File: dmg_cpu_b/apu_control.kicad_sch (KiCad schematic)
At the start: 73 parts

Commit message: CH1 Regs page completed.
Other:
- company: (none) -> CC-BY-SA-4.0 Régis Galland & Michael Singer -- Derived work from Furrtek
- title: (none) -> DMG CPU B
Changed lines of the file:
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@@
 (kicad_sch (version 20211123) (generator eeschema)
   (paper "A3")
+  (title_block
+    (title "DMG CPU B")
+    (date "2022-03-12")
+    (rev "0")
+    (company "CC-BY-SA-4.0 Régis Galland & Michael Singer -- Derived work from Furrtek")
+    (comment 1 "https://github.com/msinger/dmg-schematics")
+  )
   (junction (at 300.355 128.905) (diameter 0) (color 0 0 0 0)
   )

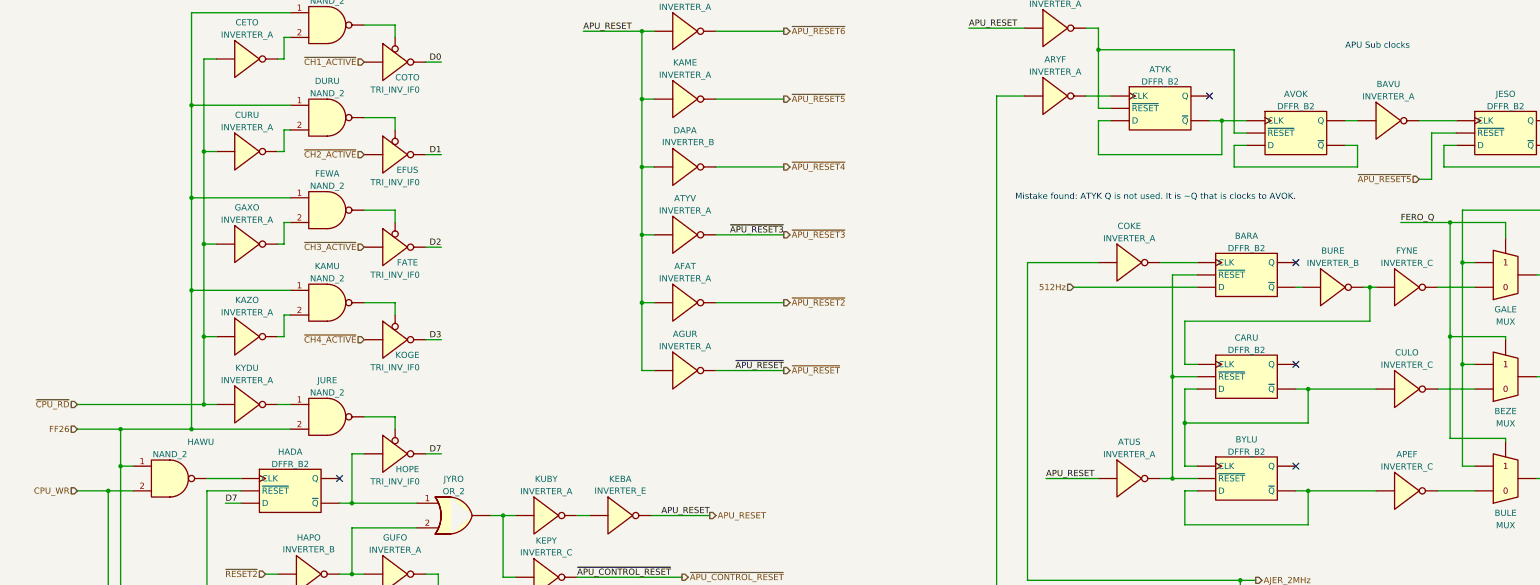
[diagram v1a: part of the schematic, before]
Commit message: CH2 Reg page added.
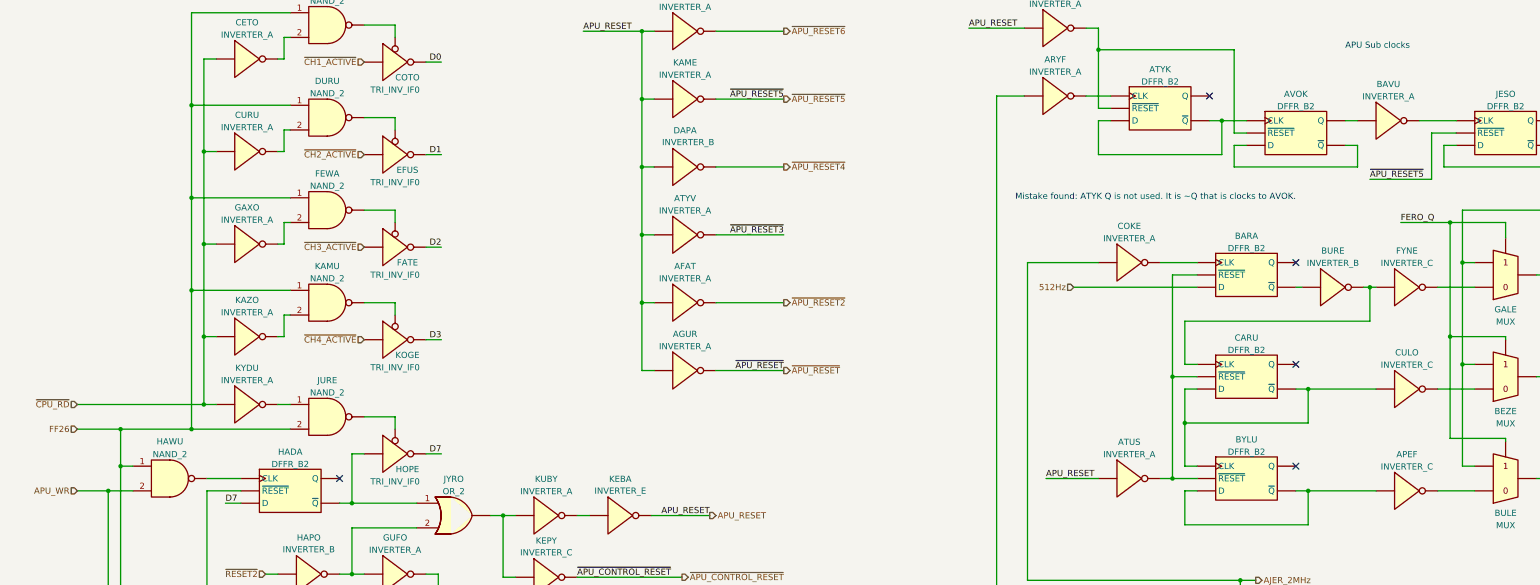
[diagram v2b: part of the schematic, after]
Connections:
- net CPU_WR renamed APU_WR
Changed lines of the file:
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@@
     (stroke (width 0) (type default) (color 0 0 0 0))
   )
-  (wire (pts (xy 323.215 85.725) (xy 325.755 85.725))
+  (wire (pts (xy 313.055 85.725) (xy 325.755 85.725))
     (stroke (width 0) (type default) (color 0 0 0 0))
   )
@@
     (effects (font (size 1.27 1.27)) (justify left bottom))
   )
+  (label "~{APU_RESET5}" (at 313.055 85.725 0)
+    (effects (font (size 1.27 1.27)) (justify left bottom))
+  )
   (label "APU_RESET" (at 177.165 154.94 180)
     (effects (font (size 1.27 1.27)) (justify right bottom))
@@
   )
   (label "D6" (at 88.9 268.605 180)
+    (effects (font (size 1.27 1.27)) (justify right bottom))
+  )
+  (label "~{APU_RESET5}" (at 192.405 69.215 180)
     (effects (font (size 1.27 1.27)) (justify right bottom))
   )
@@
     (effects (font (size 1.27 1.27)) (justify left))
   )
-  (hierarchical_label "CPU_WR" (shape input) (at 46.99 149.86 180)
+  (hierarchical_label "APU_WR" (shape input) (at 46.99 149.86 180)
     (effects (font (size 1.27 1.27)) (justify right))
   )
@@
   )
   (hierarchical_label "JESO_512K" (shape output) (at 369.57 73.66 0)
-    (effects (font (size 1.27 1.27)) (justify left))
-  )
-  (hierarchical_label "~{APU_RESET5}" (shape input) (at 323.215 85.725 180)
-    (effects (font (size 1.27 1.27)) (justify right))
-  )
-  (hierarchical_label "~{APU_RESET3}" (shape output) (at 192.405 97.155 0)
     (effects (font (size 1.27 1.27)) (justify left))
   )
@@
   (symbol (lib_id "DMG_CPU_Cells:NAND_2") (at 66.04 147.32 0) (unit 1)
     (in_bom yes) (on_board yes)
-    (property "Reference" "HAWU" (id 0) (at 72.39 139.8102 0))
+    (property "Reference" "HAWU" (id 0) (at 66.04 139.7 0))
     (property "Value" "NAND_2" (id 1) (at 66.04 142.3471 0))
     (property "Footprint" "" (id 2) (at 66.04 147.32 0)

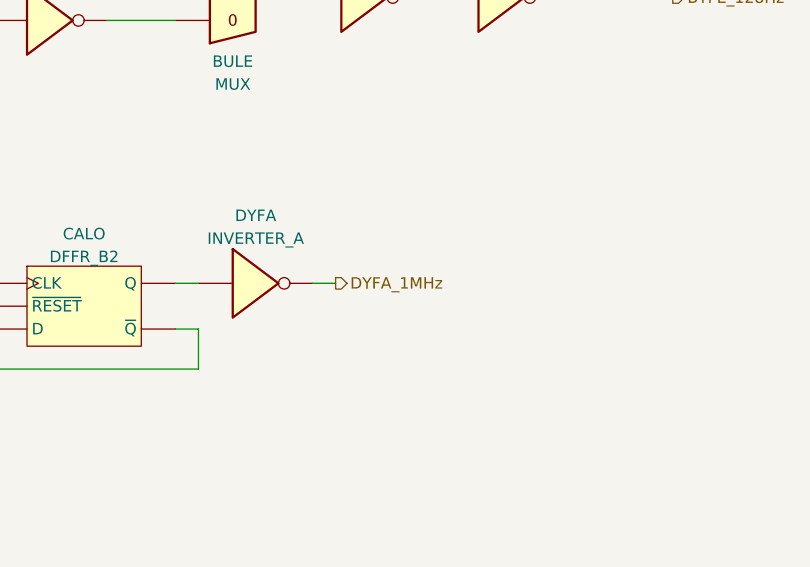
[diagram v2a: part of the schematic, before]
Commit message: channel 1 page added
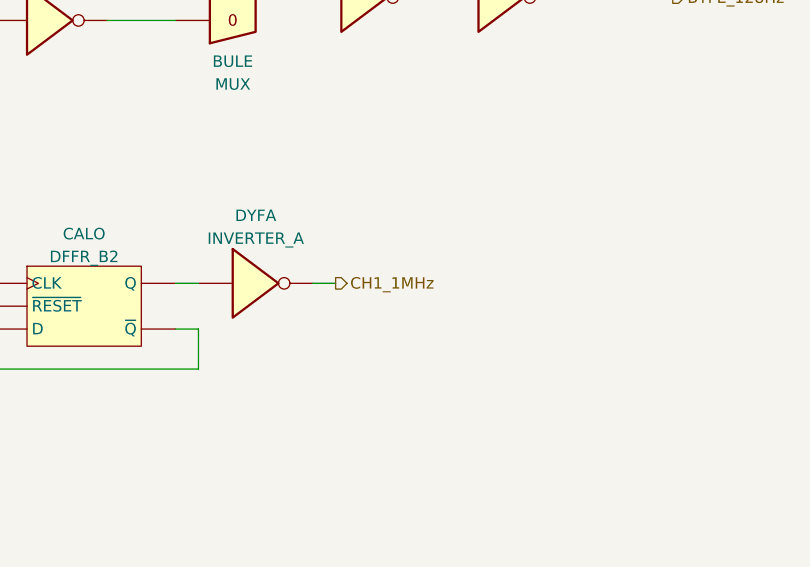
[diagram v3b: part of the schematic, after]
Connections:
- net DYFA_1MHz renamed CH1_1MHz
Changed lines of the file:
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@@
     (effects (font (size 1.27 1.27)) (justify left))
   )
-  (hierarchical_label "DYFA_1MHz" (shape output) (at 352.425 179.07 0)
+  (hierarchical_label "CH1_1MHz" (shape output) (at 352.425 179.07 0)
     (effects (font (size 1.27 1.27)) (justify left))
   )

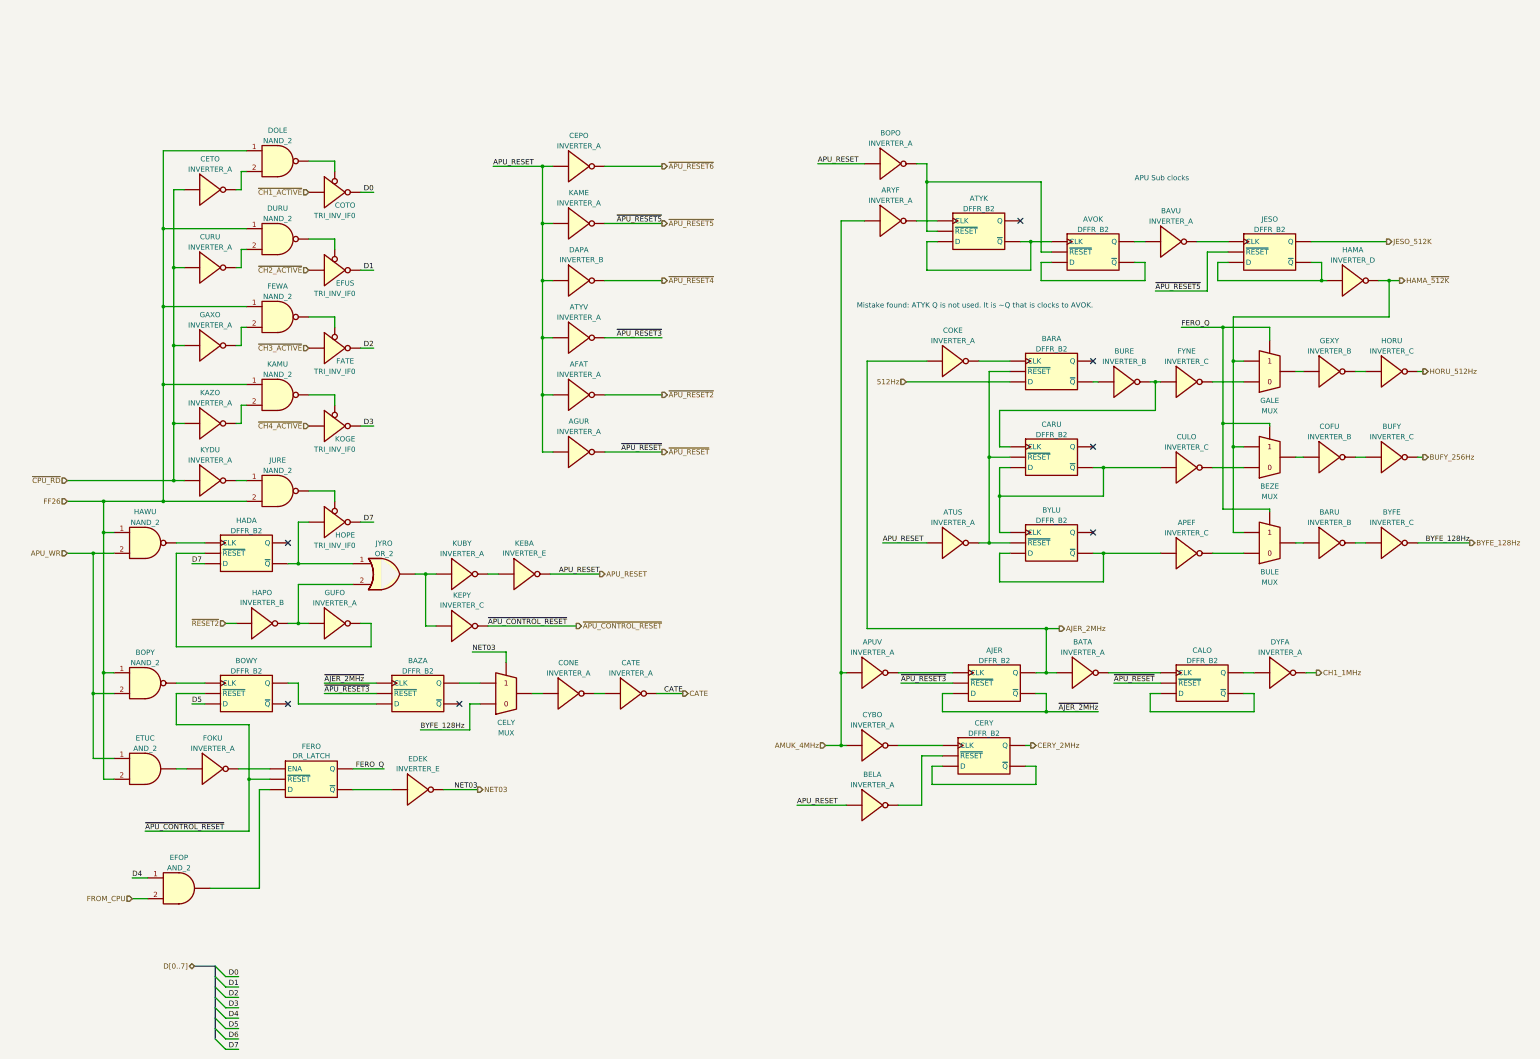
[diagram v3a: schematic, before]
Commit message: Channel 2 + Channel 3 added. Channel 3 fits on 2 sheets.
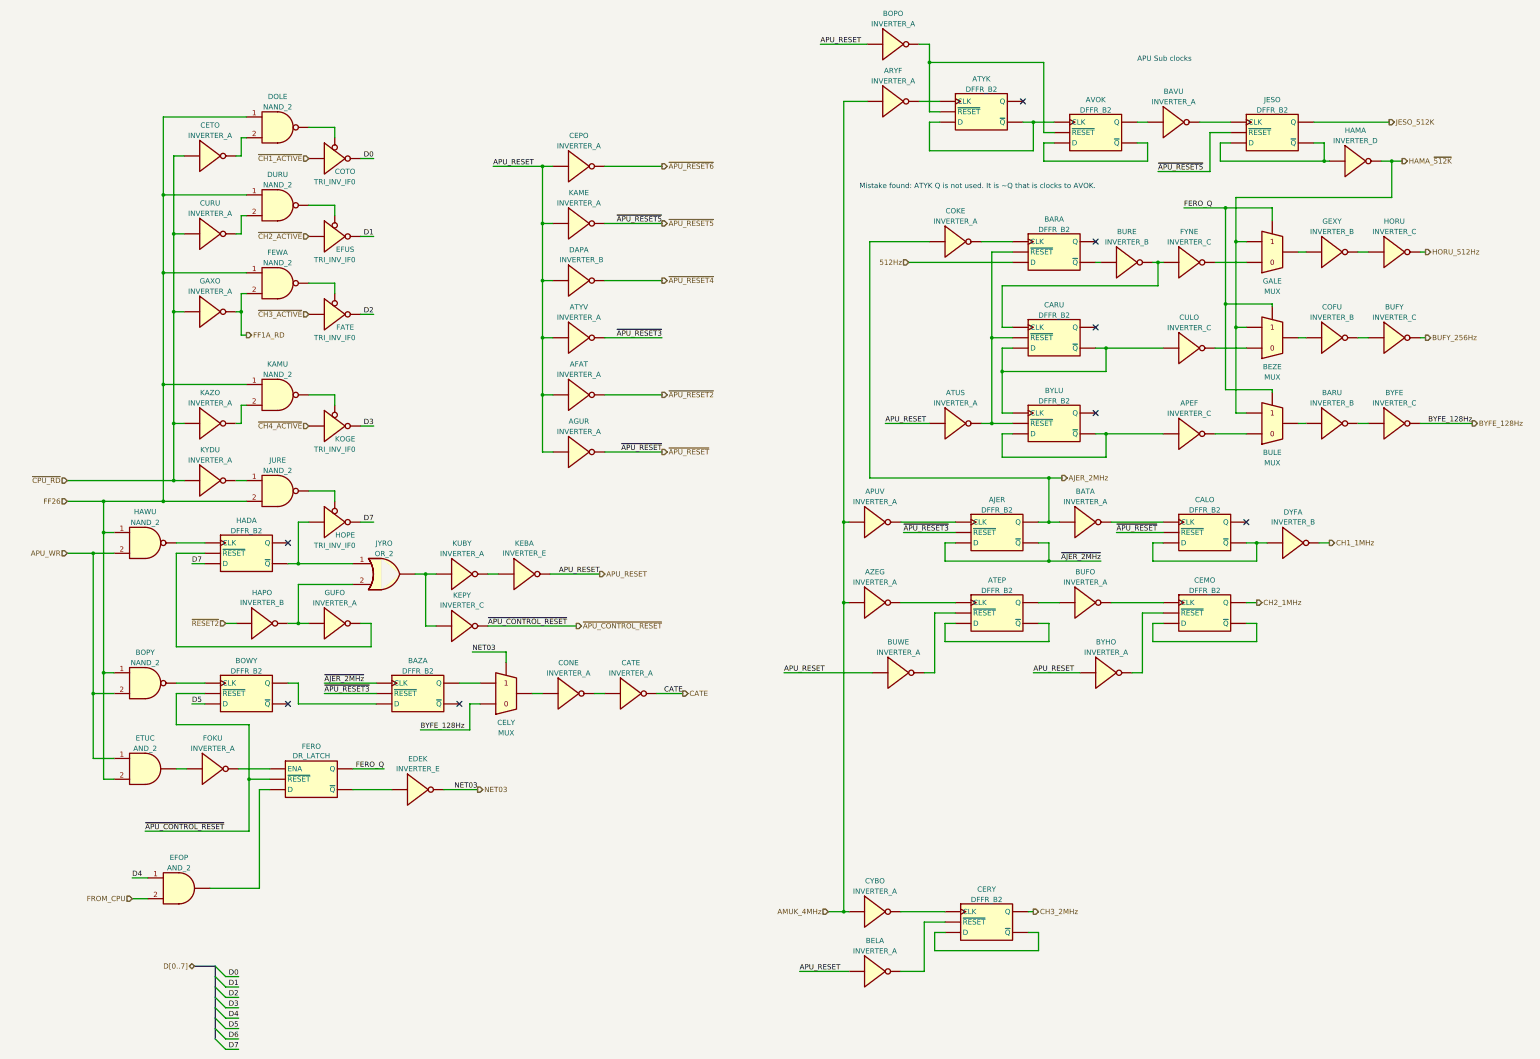
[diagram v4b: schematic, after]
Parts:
- added ATEP, CEMO: DFFR_B2, symbol DMG_CPU_Cells:DFFR_B2
- added AZEG, BUFO, BUWE, BYHO: INVERTER_A, symbol DMG_CPU_Cells:INVERTER_A
- DYFA: value INVERTER_A -> INVERTER_B; symbol DMG_CPU_Cells:INVERTER_A -> DMG_CPU_Cells:INVERTER_B
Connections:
- net AMUK_4MHz: now also AZEG.1
- net APU_RESET: now also BUWE.1, BYHO.1
- net at CALO.3 (D), CALO.5 (~{Q}): now also DYFA.1
- net at CALO.6 (Q): no longer DYFA.1
- net FF1A_RD: now reaches FEWA.2, GAXO.2
- net CERY_2MHz renamed CH3_2MHz
- new net: ATEP.6 (Q), BUFO.1
- new net: BUFO.2, CEMO.1 (CLK)
- new net: ATEP.1 (CLK), AZEG.2
- new net: BYHO.2, CEMO.2 (~{RESET}), CEMO.4 (~{RESET})
- new net: CEMO.3 (D), CEMO.5 (~{Q})
- new net: ATEP.2 (~{RESET}), ATEP.4 (~{RESET}), BUWE.2
- new net: ATEP.3 (D), ATEP.5 (~{Q})
- new net CH2_1MHz: CEMO.6 (Q)
- no-connect marks 7 -> 8
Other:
- moved on the sheet: AJER, APEF, APUV, ARYF, ATUS, ATYK, AVOK, BARA, BARU, BATA, BAVU, BELA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

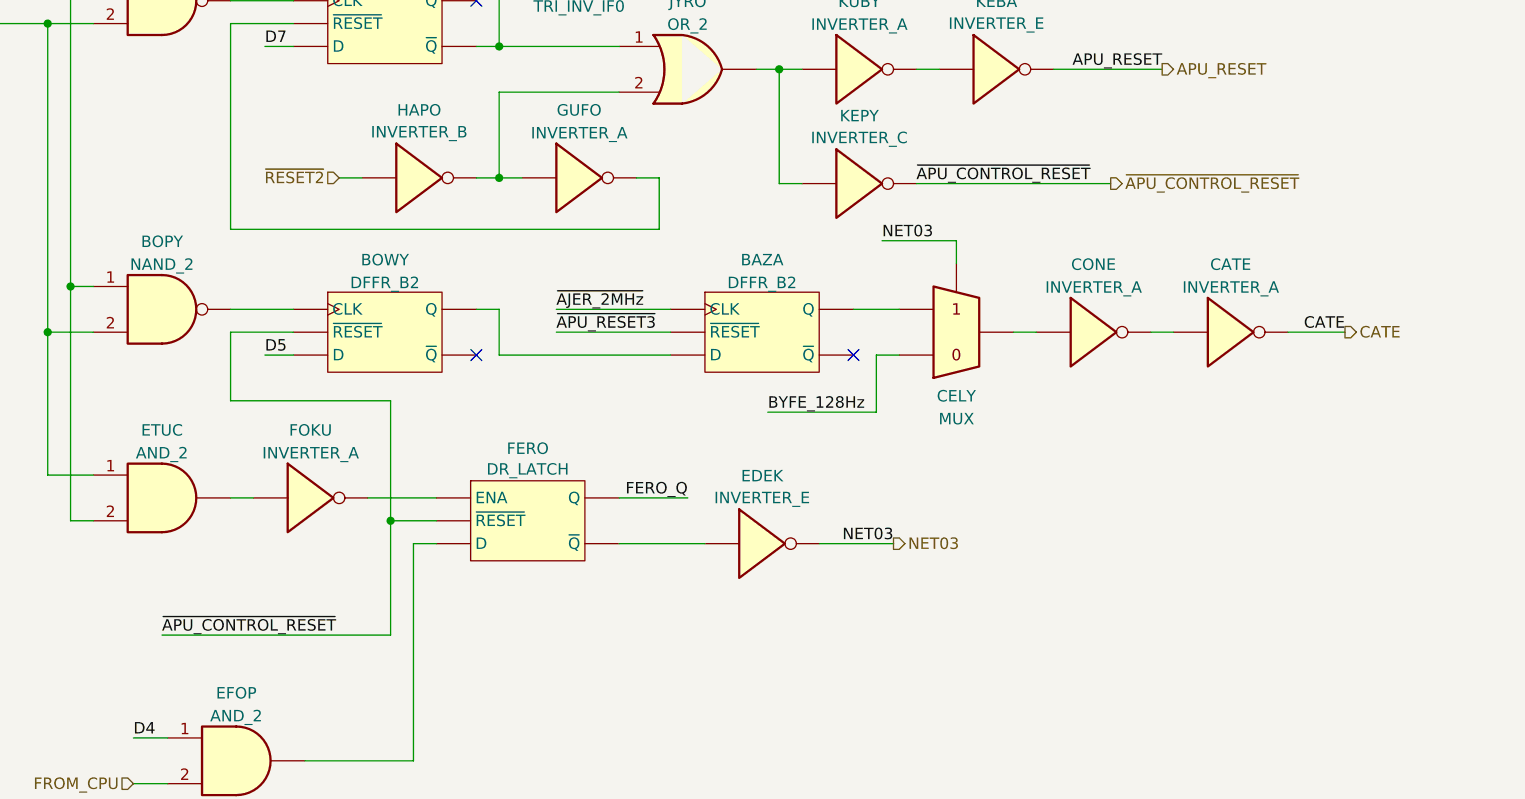
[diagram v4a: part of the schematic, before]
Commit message: fixes made following review
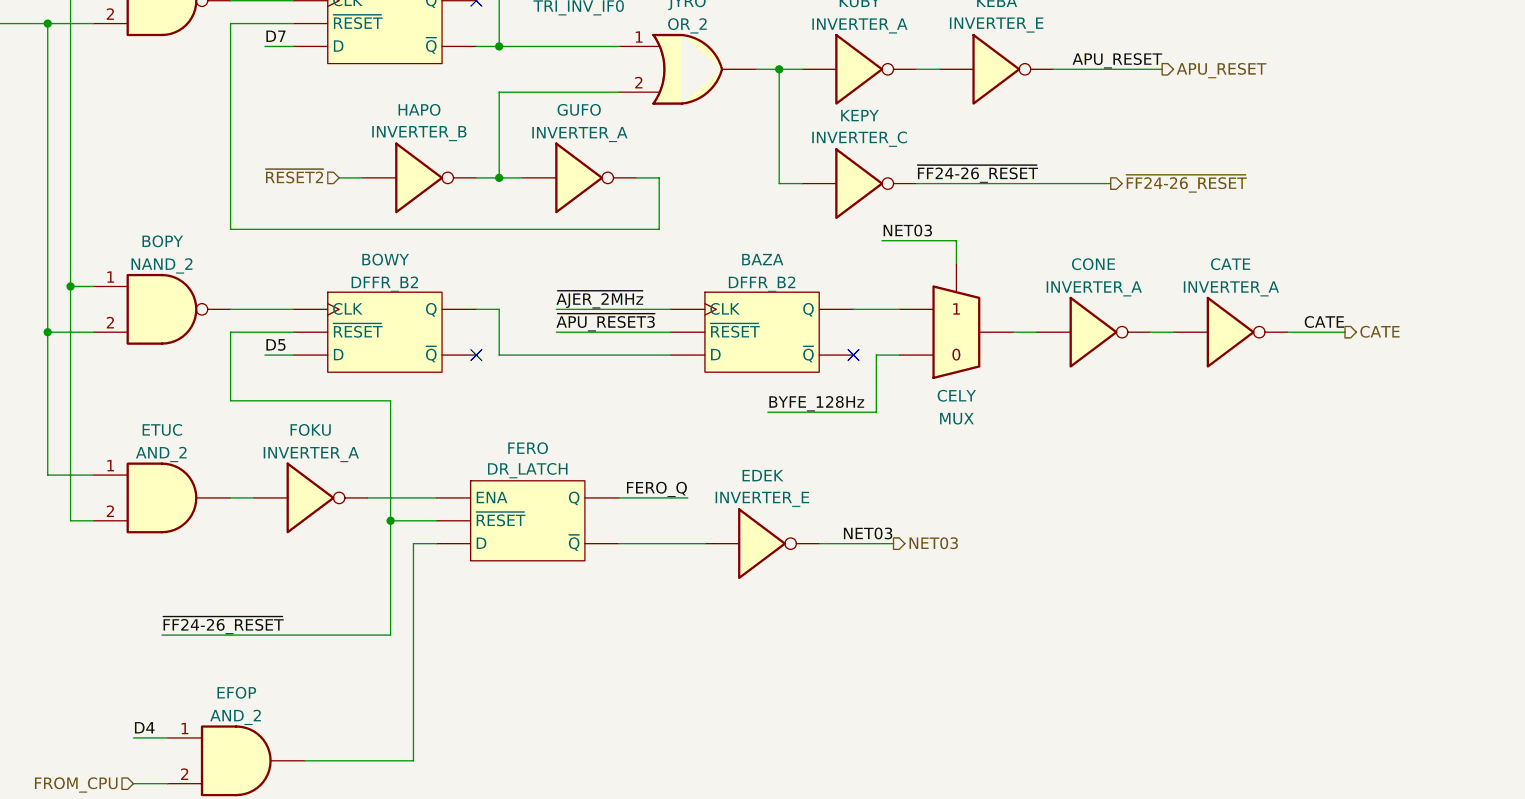
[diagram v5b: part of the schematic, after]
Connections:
- net ~{APU_CONTROL_RESET} renamed ~{FF24-26_RESET}
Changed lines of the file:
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@@
     (effects (font (size 1.27 1.27)) (justify right bottom))
   )
-  (label "~{APU_CONTROL_RESET}" (at 149.86 167.64 0)
+  (label "~{FF24-26_RESET}" (at 149.86 167.64 0)
     (effects (font (size 1.27 1.27)) (justify left bottom))
   )
@@
     (effects (font (size 1.27 1.27)) (justify right bottom))
   )
-  (label "~{APU_CONTROL_RESET}" (at 66.04 217.805 0)
+  (label "~{FF24-26_RESET}" (at 66.04 217.805 0)
     (effects (font (size 1.27 1.27)) (justify left bottom))
   )
@@
     (effects (font (size 1.27 1.27)) (justify left))
   )
-  (hierarchical_label "~{APU_CONTROL_RESET}" (shape output) (at 171.45 167.64 0)
+  (hierarchical_label "~{FF24-26_RESET}" (shape output) (at 171.45 167.64 0)
     (effects (font (size 1.27 1.27)) (justify left))
   )
